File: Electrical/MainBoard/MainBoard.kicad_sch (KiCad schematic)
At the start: 19 parts, among them J1 SNAP Program, SW1 Reset, U1 PIC32MZ2048EFH144-I/PL

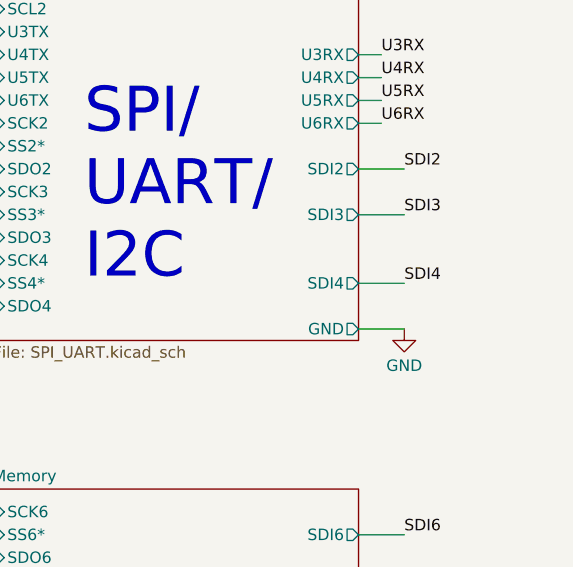
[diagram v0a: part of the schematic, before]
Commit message: Change some connections to picoblade, add env sensor connector
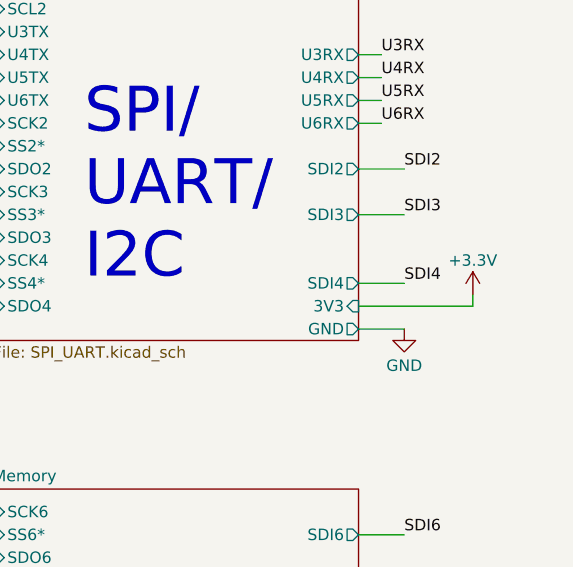
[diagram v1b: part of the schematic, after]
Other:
- sheet SPI_UART ports: added 3V3; removed none
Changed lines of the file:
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@@
 	(title_block
 		(title "MCU Controller")
-		(date "2025-06-11")
-		(rev "0.3")
+		(date "2025-08-06")
+		(rev "0.4")
 		(company "satomm@stanford.edu")
 		(comment 1 "Department of Civil and Environmental Engineering")
@@
 	(wire
 		(pts
+			(xy 398.78 134.62) (xy 411.48 134.62)
+		)
+		(stroke
+			(width 0)
+			(type default)
+		)
+	)
+	(wire
+		(pts
 			(xy 298.45 157.48) (xy 307.975 157.48)
 		)
@@
 	(wire
 		(pts
+			(xy 411.48 134.62) (xy 411.48 133.35)
+		)
+		(stroke
+			(width 0)
+			(type default)
+		)
+	)
+	(wire
+		(pts
 			(xy 146.05 182.88) (xy 156.21 182.88)
 		)
@@
 	)
 	(symbol
+		(lib_id "power:+3.3V")
+		(at 411.48 133.35 0)
+		(unit 1)
+		(exclude_from_sim no)
+		(in_bom yes)
+		(on_board yes)
+		(dnp no)
+		(property "Reference" "#PWR048"
+			(at 411.48 137.16 0)
+			(effects
+				(font
+					(size 1.27 1.27)
+				)
+				(hide yes)
+			)
+		)
+		(property "Value" "+3.3V"
+			(at 411.48 129.54 0)
+			(effects
+				(font
+					(size 1.27 1.27)
+				)
+			)
+		)
+		(property "Footprint" ""
+			(at 411.48 133.35 0)
+			(effects
+				(font
+					(size 1.27 1.27)
+				)
+				(hide yes)
+			)
+		)
+		(property "Datasheet" ""
+			(at 411.48 133.35 0)
+			(effects
+				(font
+					(size 1.27 1.27)
+				)
+				(hide yes)
+			)
+		)
+		(property "Description" ""
+			(at 411.48 133.35 0)
+			(effects
+				(font
+					(size 1.27 1.27)
+				)
+			)
+		)
+		(pin "1"
+		)
+		(instances
+			(project "MainBoard"
+				(path "/bd24c4db-4e36-4117-bd4f-5228ef241da9"
+					(reference "#PWR048")
+					(unit 1)
+				)
+			)
+		)
+	)
+	(symbol
 		(lib_id "Device:C")
 		(at 139.7 118.11 0)
@@
 			)
 		)
+		(pin "3V3" input
+			(at 398.78 134.62 0)
+			(effects
+				(font
+					(size 1.27 1.27)
+				)
+				(justify right)
+			)
+		)

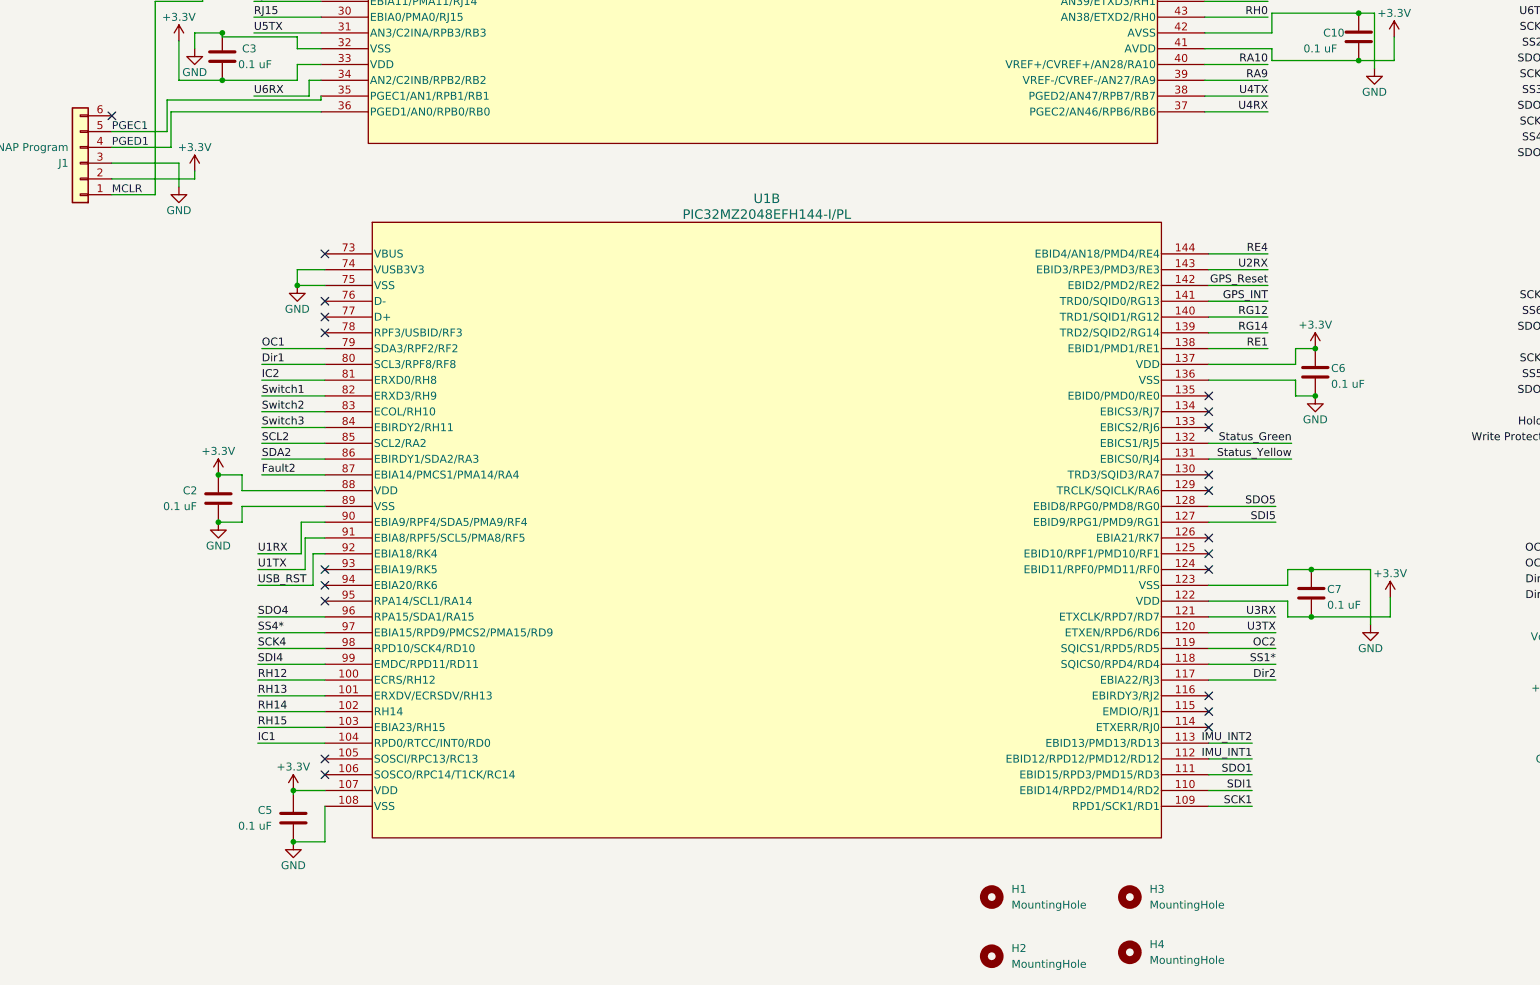
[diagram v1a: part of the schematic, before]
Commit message: Use more molex picoblades and make schematic prettier
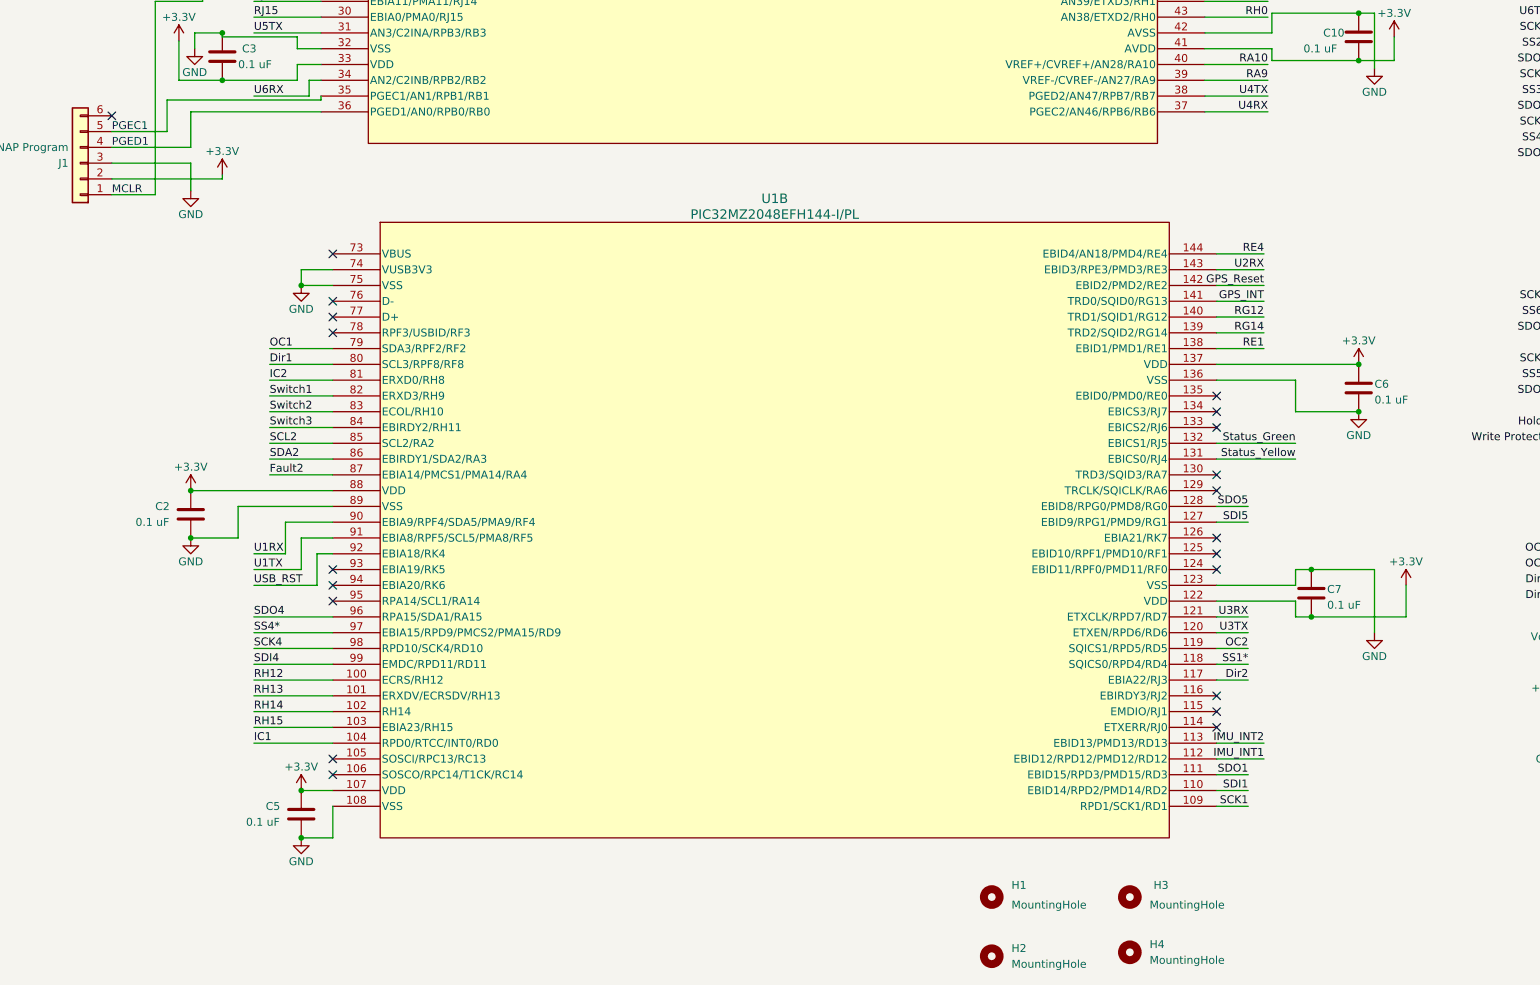
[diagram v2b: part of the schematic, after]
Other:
- moved on the sheet: C2, C5, C6, U1B
